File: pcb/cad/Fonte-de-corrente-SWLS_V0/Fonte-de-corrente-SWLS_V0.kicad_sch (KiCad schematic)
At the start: 29 parts, among them J1 Jack-DC, SW1 SW_DIP_x01, U1 LM7805, U2 LT3080xST, U3 LT3092xST, U4 LT3092xST, U5 74AHC1G04, U6 TS5A21366, U7 TS5A21366, U8 TS5A21366, U9 TS5A21366

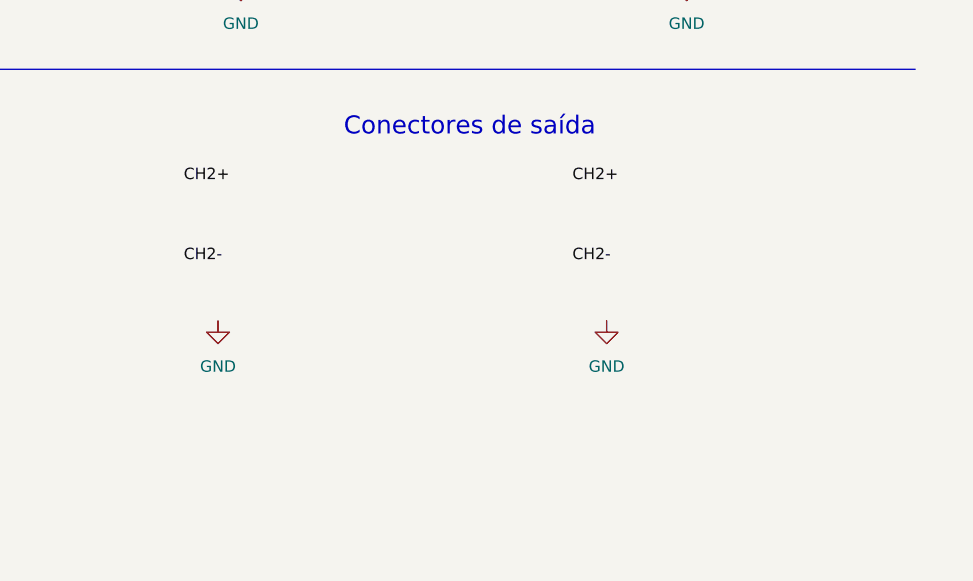
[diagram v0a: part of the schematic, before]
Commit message: Atualização do circuito esquemático, adição dos conectores lemo ff4.0s
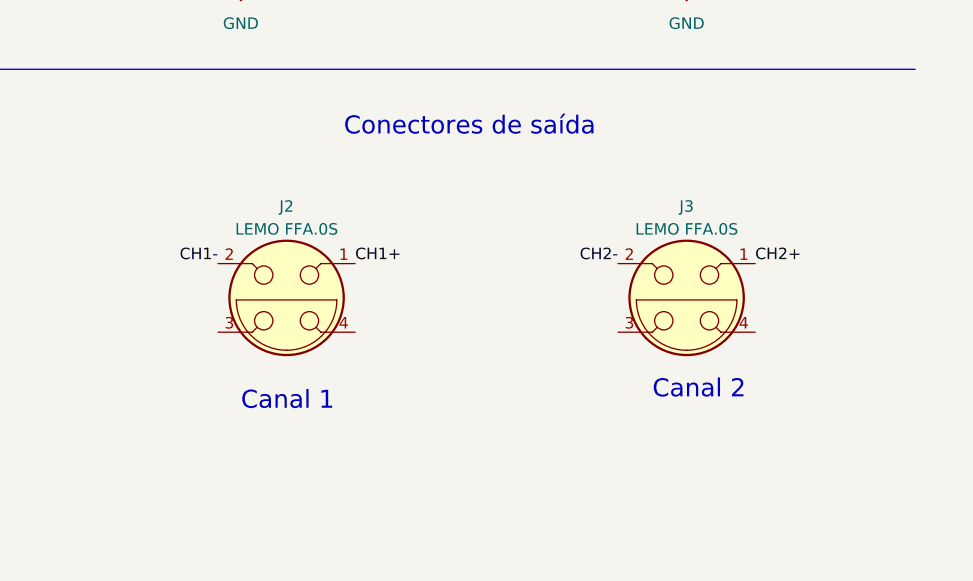
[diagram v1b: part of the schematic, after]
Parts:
- added J2, J3: LEMO FFA.0S, symbol Connector:LEMO4
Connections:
- net CH1+: now also J2.1
- net CH1-: now also J2.2
- net CH2+: now also J3.1
- net CH2-: now also J3.2
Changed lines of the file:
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@@
+    (effects (font (size 2 2)) (justify left bottom))
+  )
+  (text "Canal 2" (at 255.27 157.48 0)
     (effects (font (size 2 2)) (justify left bottom))
   )
@@
     (effects (font (size 2 2)) (justify left bottom))
   )
+  (text "Canal 1 " (at 209.55 158.75 0)
+    (effects (font (size 2 2)) (justify left bottom))
+  )
   (text "Chaves analógicas para inversão de polaridade de corrente "
     (at 186.69 19.05 0)
@@
     (effects (font (size 1.27 1.27)) (justify left bottom))
   )
-  (label "CH2+" (at 246.38 133.35 0) (fields_autoplaced)
-    (effects (font (size 1.27 1.27)) (justify left bottom))
-  )
   (label "VIN" (at 52.07 35.56 0) (fields_autoplaced)
     (effects (font (size 1.27 1.27)) (justify left bottom))
@@
     (effects (font (size 1.27 1.27)) (justify right bottom))
   )
-  (label "CH2-" (at 203.2 142.24 0) (fields_autoplaced)
-    (effects (font (size 1.27 1.27)) (justify left bottom))
+  (label "CH1-" (at 207.01 142.24 180) (fields_autoplaced)
+    (effects (font (size 1.27 1.27)) (justify right bottom))
   )
   (label "~{IN}" (at 246.38 91.44 180) (fields_autoplaced)
@@
     (effects (font (size 1.27 1.27)) (justify left bottom))
   )
-  (label "CH2+" (at 203.2 133.35 0) (fields_autoplaced)
+  (label "CH1+" (at 222.25 142.24 0) (fields_autoplaced)
     (effects (font (size 1.27 1.27)) (justify left bottom))
   )
@@
     (effects (font (size 1.27 1.27)) (justify left bottom))
   )
-  (label "CH2-" (at 246.38 142.24 0) (fields_autoplaced)
-    (effects (font (size 1.27 1.27)) (justify left bottom))
+  (label "CH2-" (at 251.46 142.24 180) (fields_autoplaced)
+    (effects (font (size 1.27 1.27)) (justify right bottom))
   )
   (label "CH1-" (at 270.51 53.34 0) (fields_autoplaced)
@@
   )
   (label "1mADC_CH2" (at 158.75 74.93 0) (fields_autoplaced)
+    (effects (font (size 1.27 1.27)) (justify left bottom))
+  )
+  (label "CH2+" (at 266.7 142.24 0) (fields_autoplaced)
     (effects (font (size 1.27 1.27)) (justify left bottom))
   )
@@
     )
   )
+  (symbol (lib_id "Connector:LEMO4") (at 259.08 146.05 0) (unit 1)
+    (in_bom yes) (on_board yes) (dnp no) (fields_autoplaced)
+    (property "Reference" "J3" (at 259.08 135.89 0)
+      (effects (font (size 1.27 1.27)))
+    )
+    (property "Value" "LEMO FFA.0S" (at 259.08 138.43 0)
+      (effects (font (size 1.27 1.27)))
+    )
+    (property "Footprint" "" (at 259.08 146.05 0)
+      (effects (font (size 1.27 1.27)) hide)
+    )
+    (property "Datasheet" " ~" (at 259.08 146.05 0)
+      (effects (font (size 1.27 1.27)) hide)
+    )
+    (pin "1")
+    (pin "2")
+    (pin "3")
+    (pin "4")
+    (instances
+      (project "Fonte-de-corrente-SWLS_V0"
+        (path "/485d57e1-9e59-4bdb-b543-f102996c1764"
+          (reference "J3") (unit 1)
+        )
+      )
+    )
+  )
   (symbol (lib_id "Device:C") (at 44.45 39.37 0) (unit 1)
     (in_bom yes) (on_board yes) (dnp no) (fields_autoplaced)
@@
     )
   )
+  (symbol (lib_id "Connector:LEMO4") (at 214.63 146.05 0) (unit 1)
+    (in_bom yes) (on_board yes) (dnp no) (fields_autoplaced)
+    (property "Reference" "J2" (at 214.63 135.89 0)
+      (effects (font (size 1.27 1.27)))
+    )
+    (property "Value" "LEMO FFA.0S" (at 214.63 138.43 0)
+      (effects (font (size 1.27 1.27)))
+    )
+    (property "Footprint" "" (at 214.63 146.05 0)
+      (effects (font (size 1.27 1.27)) hide)
+    )
+    (property "Datasheet" " ~" (at 214.63 146.05 0)
+      (effects (font (size 1.27 1.27)) hide)
+    )
+    (pin "1")
+    (pin "2")
+    (pin "3")
+    (pin "4")
+    (instances
+      (project "Fonte-de-corrente-SWLS_V0"
+        (path "/485d57e1-9e59-4bdb-b543-f102996c1764"
+          (reference "J2") (unit 1)
+        )
+      )
+    )
+  )
   (symbol (lib_id "power:+5VD") (at 209.55 80.01 0) (unit 1)
     (in_bom yes) (on_board yes) (dnp no) (fields_autoplaced)
@@
         (path "/485d57e1-9e59-4bdb-b543-f102996c1764"
           (reference "R5") (unit 1)
-        )
-      )
-    )
-  )
-  (symbol (lib_name "GND_2") (lib_id "power:GND") (at 250.19 148.59 0) (unit 1)
-    (in_bom yes) (on_board yes) (dnp no) (fields_autoplaced)
-    (property "Reference" "#PWR026" (at 250.19 154.94 0)
-      (effects (font (size 1.27 1.27)) hide)
-    )
-    (property "Value" "GND" (at 250.19 153.67 0)
-      (effects (font (size 1.27 1.27)))
-    )
-    (property "Footprint" "" (at 250.19 148.59 0)
-      (effects (font (size 1.27 1.27)) hide)
-    )
-    (property "Datasheet" "" (at 250.19 148.59 0)
-      (effects (font (size 1.27 1.27)) hide)
-    )
-    (pin "1")
-    (instances
-      (project "Fonte-de-corrente-SWLS_V0"
-        (path "/485d57e1-9e59-4bdb-b543-f102996c1764"
-          (reference "#PWR026") (unit 1)
         )
       )
@@
         )
       )
-    )
-  )
-  (symbol (lib_name "GND_2") (lib_id "power:GND") (at 207.01 148.59 0) (unit 1)
-    (in_bom yes) (on_board yes) (dnp no) (fields_autoplaced)
-    (property "Reference" "#PWR025" (at 207.01 154.94 0)
-      (effects (font (size 1.27 1.27)) hide)
-    )
-    (property "Value" "GND" (at 207.01 153.67 0)
-      (effects (font (size 1.27 1.27)))
-    )
-    (property "Footprint" "" (at 207.01 148.59 0)
-      (effects (font (size 1.27 1.27)) hide)
-    )
-    (property "Datasheet" "" (at 207.01 148.59 0)
-      (effects (font (size 1.27 1.27)) hide)
-    )
-    (pin "1")
-    (instances
-      (project "Fonte-de-corrente-SWLS_V0"
-        (path "/485d57e1-9e59-4bdb-b543-f102996c1764"
-          (reference "#PWR025") (unit 1)
-        )
-      )

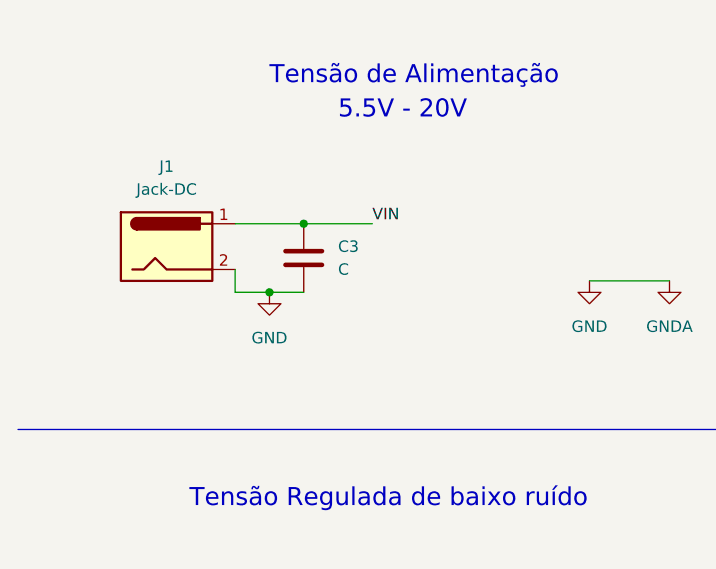
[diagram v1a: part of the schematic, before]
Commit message: Atualização do circuito esquemático, adição dos conectores lemo ff4.0s
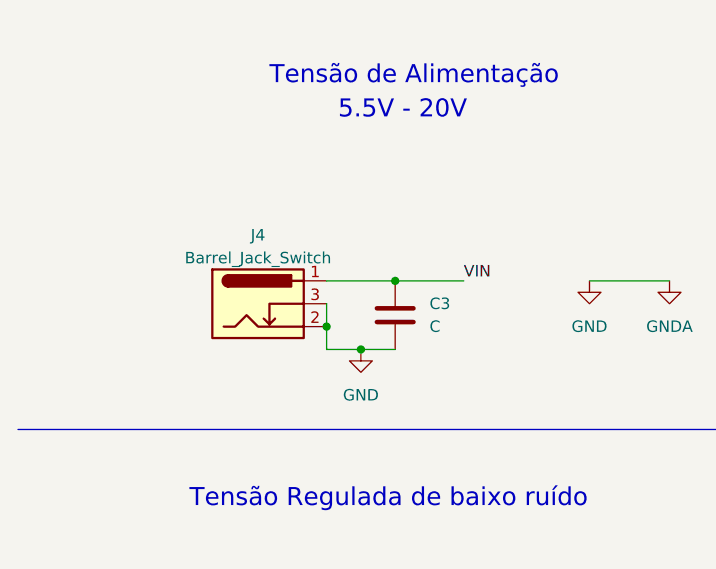
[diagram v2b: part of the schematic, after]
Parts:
- removed J1: Jack-DC, symbol Connector:Jack-DC
- added J4: Barrel_Jack_Switch, Connector_BarrelJack:BarrelJack_GCT_DCJ200-10-A_Horizontal, symbol Connector:Barrel_Jack_Switch
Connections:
- net GND: now also J4.2, J4.3
- net VIN: now also J4.1
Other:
- moved on the sheet: C3
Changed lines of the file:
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@@
   (junction (at 30.48 85.09) (diameter 0) (color 0 0 0 0)
   )
-  (junction (at 44.45 35.56) (diameter 0) (color 0 0 0 0)
+  (junction (at 54.61 41.91) (diameter 0) (color 0 0 0 0)
   )
   (junction (at 39.37 95.25) (diameter 0) (color 0 0 0 0)
@@
   (junction (at 53.34 184.15) (diameter 0) (color 0 0 0 0)
   )
-  (junction (at 40.64 43.18) (diameter 0) (color 0 0 0 0)
+  (junction (at 50.8 49.53) (diameter 0) (color 0 0 0 0)
   )
   (junction (at 151.13 46.99) (diameter 0) (color 0 0 0 0)
   )
+  (junction (at 46.99 46.99) (diameter 0) (color 0 0 0 0)
+  )
   (wire (pts (xy 138.43 158.75) (xy 142.24 158.75))
     (stroke (width 0) (type default))
@@
     (stroke (width 0) (type default))
   )
-  (wire (pts (xy 36.83 40.64) (xy 36.83 43.18))
+  (wire (pts (xy 46.99 46.99) (xy 46.99 49.53))
     (stroke (width 0) (type default))
   )
@@
     (stroke (width 0) (type default))
   )
-  (wire (pts (xy 36.83 43.18) (xy 40.64 43.18))
+  (wire (pts (xy 46.99 49.53) (xy 50.8 49.53))
     (stroke (width 0) (type default))
   )
@@
     (stroke (width 0) (type default))
   )
-  (wire (pts (xy 36.83 35.56) (xy 44.45 35.56))
+  (wire (pts (xy 46.99 41.91) (xy 54.61 41.91))
     (stroke (width 0) (type default))
   )
@@
     (stroke (width 0) (type default))
   )
+  (wire (pts (xy 46.99 44.45) (xy 46.99 46.99))
+    (stroke (width 0) (type default))
+  )
   (polyline (pts (xy 12.7 58.42) (xy 101.6 58.42))
     (stroke (width 0) (type default))
@@
     (stroke (width 0) (type default))
   )
-  (wire (pts (xy 40.64 43.18) (xy 44.45 43.18))
+  (wire (pts (xy 50.8 49.53) (xy 54.61 49.53))
     (stroke (width 0) (type default))
   )
@@
     (stroke (width 0) (type default))
   )
-  (wire (pts (xy 44.45 35.56) (xy 52.07 35.56))
+  (wire (pts (xy 54.61 41.91) (xy 62.23 41.91))
     (stroke (width 0) (type default))
   )
@@
     (effects (font (size 1.27 1.27)) (justify left bottom))
   )
-  (label "VIN" (at 52.07 35.56 0) (fields_autoplaced)
+  (label "VIN" (at 62.23 41.91 0) (fields_autoplaced)
     (effects (font (size 1.27 1.27)) (justify left bottom))
   )
@@
     )
   )
-  (symbol (lib_id "Device:C") (at 44.45 39.37 0) (unit 1)
-    (in_bom yes) (on_board yes) (dnp no) (fields_autoplaced)
-    (property "Reference" "C3" (at 48.26 38.0999 0)
-      (effects (font (size 1.27 1.27)) (justify left))
-    )
-    (property "Value" "C" (at 48.26 40.6399 0)
-      (effects (font (size 1.27 1.27)) (justify left))
-    )
-    (property "Footprint" "" (at 45.4152 43.18 0)
-      (effects (font (size 1.27 1.27)) hide)
-    )
-    (property "Datasheet" "~" (at 44.45 39.37 0)
+  (symbol (lib_id "Device:C") (at 54.61 45.72 0) (unit 1)
+    (in_bom yes) (on_board yes) (dnp no) (fields_autoplaced)
+    (property "Reference" "C3" (at 58.42 44.4499 0)
+      (effects (font (size 1.27 1.27)) (justify left))
+    )
+    (property "Value" "C" (at 58.42 46.9899 0)
+      (effects (font (size 1.27 1.27)) (justify left))
+    )
+    (property "Footprint" "" (at 55.5752 49.53 0)
+      (effects (font (size 1.27 1.27)) hide)
+    )
+    (property "Datasheet" "~" (at 54.61 45.72 0)
       (effects (font (size 1.27 1.27)) hide)
     )
@@
         (path "/485d57e1-9e59-4bdb-b543-f102996c1764"
           (reference "#PWR018") (unit 1)
-        )
-      )
-    )
-  )
-  (symbol (lib_id "Connector:Jack-DC") (at 29.21 38.1 0) (unit 1)
-    (in_bom yes) (on_board yes) (dnp no) (fields_autoplaced)
-    (property "Reference" "J1" (at 29.21 29.21 0)
-      (effects (font (size 1.27 1.27)))
-    )
-    (property "Value" "Jack-DC" (at 29.21 31.75 0)
-      (effects (font (size 1.27 1.27)))
-    )
-    (property "Footprint" "" (at 30.48 39.116 0)
-      (effects (font (size 1.27 1.27)) hide)
-    )
-    (property "Datasheet" "~" (at 30.48 39.116 0)
-      (effects (font (size 1.27 1.27)) hide)
-    )
-    (pin "1")
-    (pin "2")
-    (instances
-      (project "Fonte-de-corrente-SWLS_V0"
-        (path "/485d57e1-9e59-4bdb-b543-f102996c1764"
-          (reference "J1") (unit 1)
         )
       )
@@
     )
   )
-  (symbol (lib_name "GND_3") (lib_id "power:GND") (at 40.64 43.18 0) (unit 1)
-    (in_bom yes) (on_board yes) (dnp no) (fields_autoplaced)
-    (property "Reference" "#PWR013" (at 40.64 49.53 0)
-      (effects (font (size 1.27 1.27)) hide)
-    )
-    (property "Value" "GND" (at 40.64 48.26 0)
-      (effects (font (size 1.27 1.27)))
-    )
-    (property "Footprint" "" (at 40.64 43.18 0)
-      (effects (font (size 1.27 1.27)) hide)
-    )
-    (property "Datasheet" "" (at 40.64 43.18 0)
+  (symbol (lib_name "GND_3") (lib_id "power:GND") (at 50.8 49.53 0) (unit 1)
+    (in_bom yes) (on_board yes) (dnp no) (fields_autoplaced)
+    (property "Reference" "#PWR013" (at 50.8 55.88 0)
+      (effects (font (size 1.27 1.27)) hide)
+    )
+    (property "Value" "GND" (at 50.8 54.61 0)
+      (effects (font (size 1.27 1.27)))
+    )
+    (property "Footprint" "" (at 50.8 49.53 0)
+      (effects (font (size 1.27 1.27)) hide)
+    )
+    (property "Datasheet" "" (at 50.8 49.53 0)
       (effects (font (size 1.27 1.27)) hide)
     )
@@
         )
       )
+    )
+  )
+  (symbol (lib_id "Connector:Barrel_Jack_Switch") (at 39.37 44.45 0) (unit 1)
+    (in_bom yes) (on_board yes) (dnp no) (fields_autoplaced)
+    (property "Reference" "J4" (at 39.37 36.83 0)
+      (effects (font (size 1.27 1.27)))
+    )
+    (property "Value" "Barrel_Jack_Switch" (at 39.37 39.37 0)
+      (effects (font (size 1.27 1.27)))
+    )
+    (property "Footprint" "Connector_BarrelJack:BarrelJack_GCT_DCJ200-10-A_Horizontal" (at 40.64 45.466 0)
+      (effects (font (size 1.27 1.27)) hide)
+    )
+    (property "Datasheet" "https://www.cuidevices.com/product/resource/pj-002ah.pdf" (at 40.64 45.466 0)
+      (effects (font (size 1.27 1.27)) hide)
+    )
+    (property "Numero do produto" "PJ-002AH" (at 39.37 44.45 0)
+      (effects (font (size 1.27 1.27)) hide)
+    )
+    (pin "1")
+    (pin "2")
+    (pin "3")
+    (instances
+      (project "Fonte-de-corrente-SWLS_V0"
+        (path "/485d57e1-9e59-4bdb-b543-f102996c1764"
+          (reference "J4") (unit 1)
+        )
+      )
